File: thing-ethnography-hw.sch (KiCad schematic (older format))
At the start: 21 parts

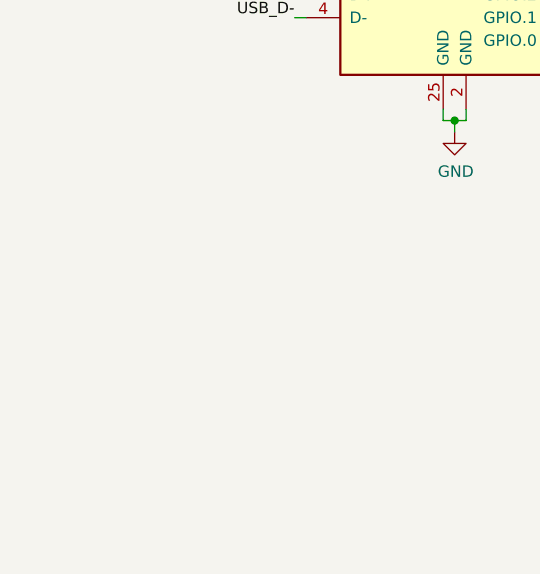
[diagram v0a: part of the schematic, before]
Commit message: Add CP2104 with custom symbol, will finish later
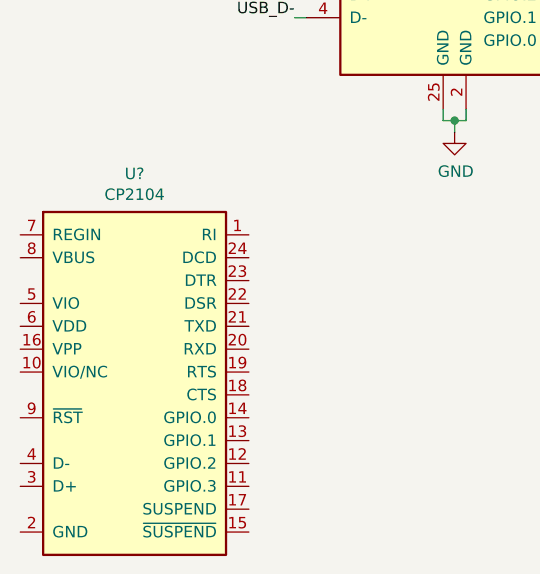
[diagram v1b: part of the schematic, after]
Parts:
- added U?: CP2104, Package_DFN_QFN:QFN-24-1EP_4x4mm_P0.5mm_EP2.6x2.6mm, symbol Interface_USB_Extra:CP2104
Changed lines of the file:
@@
 Text Notes 3200 2250 0    50   ~ 0
 PROG resistor:\n10K =  100mA\n 5K =  200mA\n 2K =  500mA\n 1K = 1000mA
+$Comp
+L Interface_USB_Extra:CP2104 U?
+U 1 1 5BA03740
+P 1500 6600
+F 0 "U?" H 1500 7367 50  0000 C CNN
+F 1 "CP2104" H 1500 7276 50  0000 C CNN
+F 2 "Package_DFN_QFN:QFN-24-1EP_4x4mm_P0.5mm_EP2.6x2.6mm" H 200 5600 50  0001 L CNN
+F 3 "https://www.silabs.com/Support%20Documents/TechnicalDocs/cp2104.pdf" H 950 7850 50  0001 C CNN
+	1    1500 6600
+	1    0    0    -1
+$EndComp
 $EndSCHEMATC

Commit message: Finish up the schematic
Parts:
- removed C? (x2): 1uF, symbol Device:C_Small
- removed C?: 4.7uF, symbol Device:C_Small
- removed D? (x2): S1JHE, symbol Device:D_Small
- removed D?: LED_Small, symbol Device:LED_Small
- removed R? (x2): 1k, symbol Device:R_Small
- removed R?: 360R, symbol Device:R_Small
- removed U?: MCP1700-3302E, Package_TO_SOT_SMD:SOT-23, symbol Regulator_Linear:MCP1700-3302E_SOT23
- removed U?: CP2102N, Package_DFN_QFN:QFN-24-1EP_4x4mm_P0.5mm_EP2.6x2.6mm, symbol Interface_USB:CP2102N-A01-GQFN24
- removed U?: MCP73831, Package_TO_SOT_SMD:SOT-23-5, symbol Battery_Management:MCP73831-2-OT
- added C2: 4.7uF, Capacitor_SMD:C_0603_1608Metric, symbol Device:C_Small
- added J1: Micro_SD_Card_Det, Connector_Card_Extra:microSD_HC_Molex_104031-0811, symbol Connector:Micro_SD_Card_Det
- added J2: Conn_12V, TerminalBlock:TerminalBlock_bornier-2_P5.08mm, symbol Connector_Generic:Conn_01x02
- added J3: Conn_Lamp, TerminalBlock:TerminalBlock_bornier-2_P5.08mm, symbol Connector_Generic:Conn_01x02
- added Q3: IRLB8721PBF, Package_TO_SOT_THT:TO-220-3_Vertical, symbol Transistor_FET:IRLB8721PBF
- added R4: 4.7K, Resistor_SMD:R_0603_1608Metric, symbol Device:R_Small
- added R5, R6: 1K, Resistor_SMD:R_0603_1608Metric, symbol Device:R_Small
- added SW3: Rotary_Encoder_Switch, Rotary_Encoder:RotaryEncoder_Alps_EC11E-Switch_Vertical_H20mm, symbol Device:Rotary_Encoder_Switch
- C1: renamed from C?; footprint (none) -> Capacitor_SMD:C_0603_1608Metric
- R1, R2, R3: renamed from R?; footprint (none) -> Resistor_SMD:R_0603_1608Metric
- SW1, SW2: renamed from SW?; footprint (none) -> Button_Switch_SMD:SW_SPST_B3U-1000P
- U1: renamed from U?; footprint XCVR_ESP32-WROVER-I -> RF_Module_Extra:ESP32-WROVER
- gave numbers to parts that had none: 3
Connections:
- net labels added: 12V_GND, 12V_VDD, ADC5, ADC6, ADC7, CAMERA_ON, CARD_CLK, CARD_CS, CARD_DET, CARD_MISO, CARD_MOSI, GPIO, MOSFET_ON, ROTARY_A, ROTARY_B, ROTARY_SW
- net labels removed: +BATT, VIN
- wire segments 112 -> 104
- no-connect marks 10 -> 19
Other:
- note removed: "PROG resistor:\n10K = 100mA\n 5K = 200mA\n 2K = 500mA\n 1K = 1000mA"
- note removed: "TODO:\n- LEDs\n- Adafruit Camera\n- SDCard\n- Battery holder\n- Analog in x3\n- Digital in x5-10\n- Potentiometer\n- On-off switch\n- Flash button\n- Reset button\n- 12V Mosfet"
- note removed: "VIN max: 6V\nOut: 250mA\nDropout: 178mV"
- moved on the sheet: C1, Q1, Q2, R1, R2, R3, SW1, SW2, U1, U2
